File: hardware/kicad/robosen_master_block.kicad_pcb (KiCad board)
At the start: 2 copper layers, 17 parts, among them J1 CONFIG_DOCK_PORT, J2 RUN_CHAIN_PORT, SW1 Knob 1 (Action), SW2 Knob 2 (Param), SW3 CONFIRM_START (Green), SW4 POWER_SWITCH, SW5 CANCEL_STOP (Red), U1 ESP32-S3-DevKitC-1, U2 TP4056_USB-C_BMS, U3 TPS63020_3.3V_BuckBoost

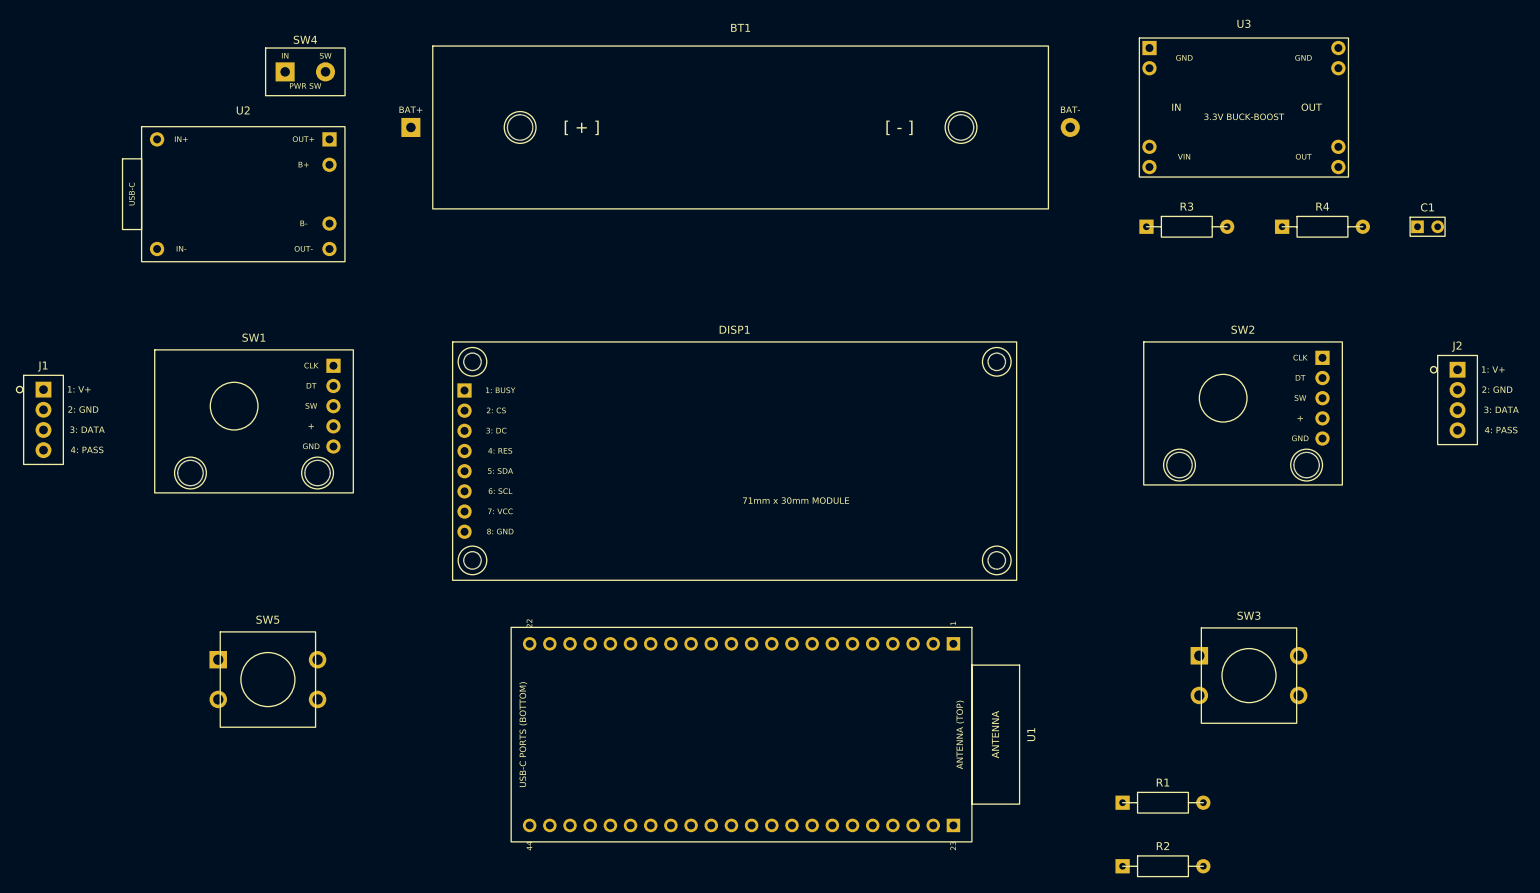
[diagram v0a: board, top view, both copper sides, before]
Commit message: feat(hardware): finalize PCB component placement and add 4x M3 mounting holes
- Positioned ESP32-S3 (U1) and 18650 battery holder (BT1) on bottom copper layer (B.Cu)
- Configured front panel component layout within 115.5 x 62 mm Edge.Cuts outline
- Added 4x locked M3 mounting holes (H1-H4) for 3D casing heat-set inserts
- Added 3D render previews and mounting enclosure specification document
- Added placement verification script and updated .gitignore for DRC reports
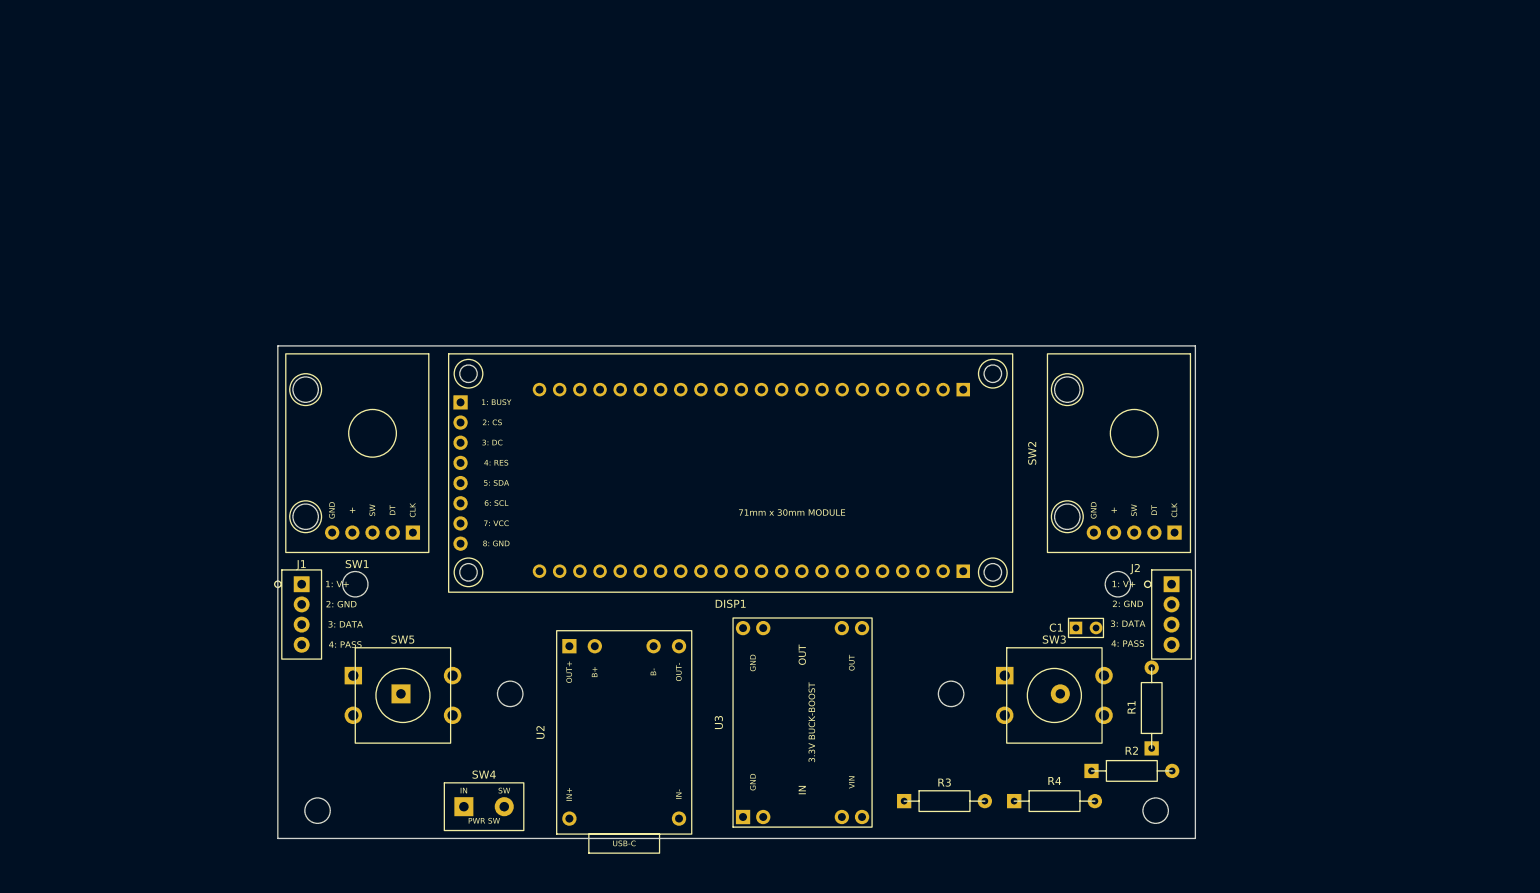
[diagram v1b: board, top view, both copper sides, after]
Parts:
- added H1: MountingHole_3.2mm_M3, MountingHole_3.2mm_M3, F.Cu at (96.2, 92.0)
- added H2: MountingHole_3.2mm_M3, MountingHole_3.2mm_M3, F.Cu at (192.2, 92.0)
- added H3: MountingHole_3.2mm_M3, MountingHole_3.2mm_M3, F.Cu at (91.5, 120.5)
- added H4: MountingHole_3.2mm_M3, MountingHole_3.2mm_M3, F.Cu at (197.0, 120.5)
- BT1, U1: moved to B.Cu
- moved U3 95.3 mm to (152.6, 109.4), turned to 90 degrees
- moved SW4 95.2 mm to (112.5, 120.0)
- moved U2 83.0 mm to (130.1, 110.7), turned to 90 degrees
- moved R4 79.8 mm to (184.3, 119.3)
- moved R3 78.5 mm to (170.4, 119.3)
- moved BT1 71.3 mm to (143.5, 105.8)
- moved C1 66.3 mm to (188.2, 97.5)
- moved J2 45.0 mm to (199.0, 92.0)
- moved J1 40.7 mm to (89.5, 92.0)
- moved U1 32.0 mm to (146.1, 78.9), turned to 90 degrees
- moved SW3 24.6 mm to (184.2, 106.0)
- moved SW5 17.1 mm to (102.2, 106.0)
- moved SW2 16.4 mm to (192.4, 75.5), turned to -90 degrees
- moved SW1 13.6 mm to (96.5, 75.5), turned to -90 degrees
- moved R2 12.6 mm to (194.0, 115.5)
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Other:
- board outline added: 115.5 x 62 mm

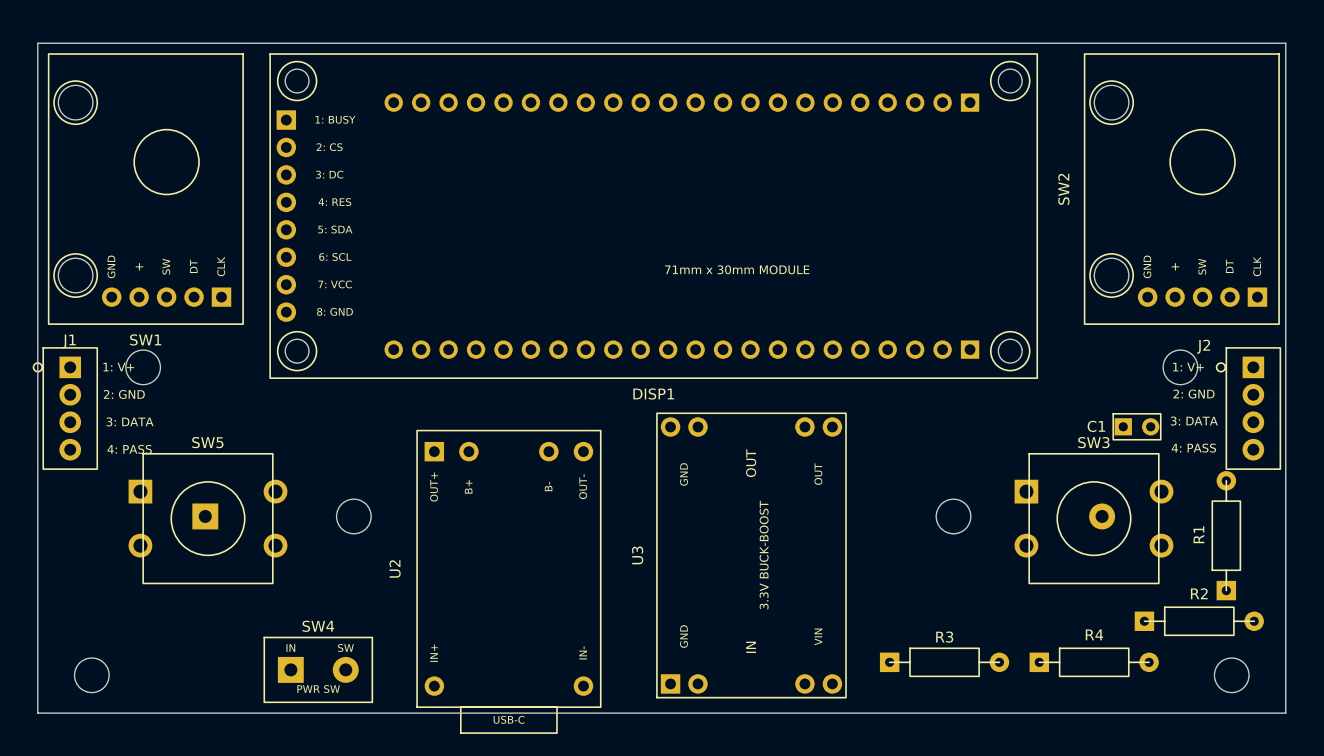
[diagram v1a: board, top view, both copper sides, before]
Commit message: feat(hardware): finalize PCB trace routing, export manufacturer gerbers, and update docs
- 100% routed 2-layer PCB layout with 0 unconnected items (KiCad DRC verified)
- Dual-layer continuous GND power planes with thermal relief spokes and automatic island removal
- 0.80 mm power traces (+3V3, /VBAT_*) and isolated /VBAT_GND for TP4056 BMS protection
- Verified >= 3.68 mm clearance around all 4 M3 mounting holes (H1-H4) for screw heads & bosses
- Completed independent dual-agent verification (Antigravity + GPT-6 Astra)
- Exported production Gerbers, Excellon drill files, and packaged robosen_master_block_gerbers.zip
- Updated documentation (mounting spec, README, TODO, PROJECT_SUMMARY) with assembly guidelines
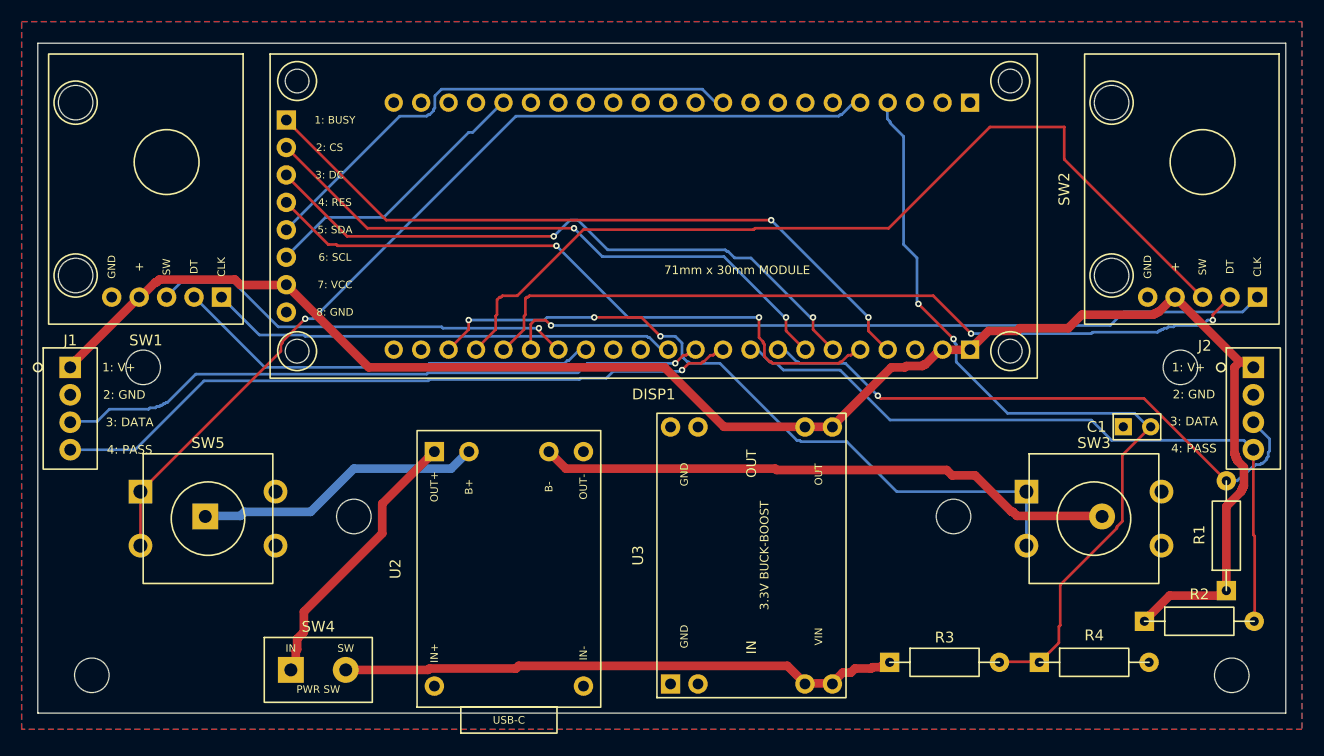
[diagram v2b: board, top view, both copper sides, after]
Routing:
- net +3V3: track 0.00 -> 157.9 mm
- net /BTN_STOP: track 0.00 -> 87.0 mm, vias 0 -> 1
- net /K2_SW: track 0.00 -> 85.7 mm
- net /BATSENSE: track 0.00 -> 77.1 mm, vias 0 -> 2
- net /K2_DT: track 0.00 -> 74.1 mm, vias 0 -> 2
- net /K2_CLK: track 0.00 -> 71.1 mm, vias 0 -> 1
- net /BTN_START: track 0.00 -> 67.7 mm, vias 0 -> 3
- net /CHAIN_RX: track 0.00 -> 66.4 mm
- net /EPD_BUSY: track 0.00 -> 65.2 mm, vias 0 -> 2
- net /CFG_TX: track 0.00 -> 64.3 mm, vias 0 -> 1
- net /EPD_RES: track 0.00 -> 61.7 mm, vias 0 -> 2
- net /CFG_RX: track 0.00 -> 60.7 mm, vias 0 -> 1
- net /EPD_DC: track 0.00 -> 59.3 mm, vias 0 -> 2
- net /EPD_CS: track 0.00 -> 56.6 mm, vias 0 -> 2
- net /CHAIN_TX: track 0.00 -> 55.3 mm, vias 0 -> 1
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- added copper zone on B.Cu, net GND
- added copper zone on F.Cu, net GND
